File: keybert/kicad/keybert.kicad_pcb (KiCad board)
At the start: 2 copper layers, 146.8 x 123 mm, 62 parts, among them J0 TRRS

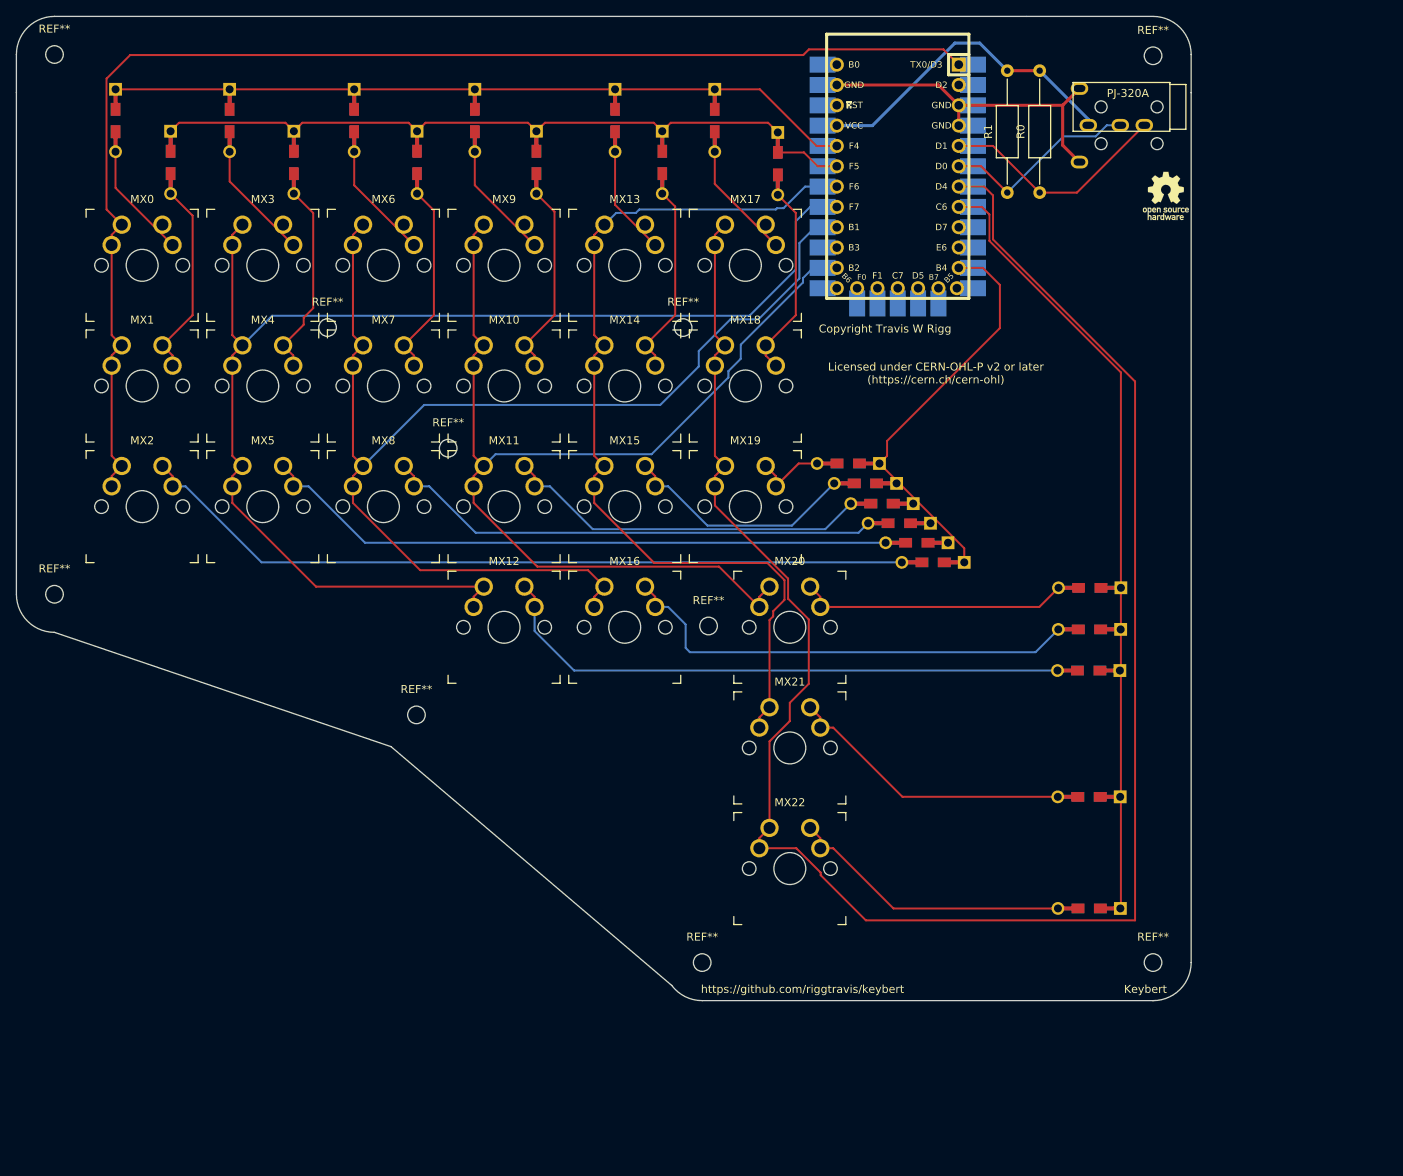
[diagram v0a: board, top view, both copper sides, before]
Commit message: feat: enforced good board geometry using FreeCAD
Parametric modeling is a wonderful thing and I'm unclear on why
KiCAD doesn't have it. Oh well, it is what is is. Using the
dimensions I obtained from the wonderful experience of performing
my parametric modeling adjustments, I finally had all of the
information I needed to get pricing for the PCBs as they are
currently designed. The results were not good. Currently,
[Aisler](https://aisler.community/t/pcb-design-rules/41) rates the
design as complex. This fails to meet the mission goal of Keybert
in a couple of ways.

Firstly, a complex PCB is an expensive PCB and an expensive PCB is
not beginner friendly. Secondly, a complex PCB is a harder to
understand and evaluate PCB and a harder to understand and evaluate
PCB is a PCB that doesn't help a biginner wrap their heads around
the sorts of decisions are present in the general world of custom
mechanical keyboards. Also, as an open source project, I feel a
certain degree of responsibility to make sure that this is as easy
to remix and remaster as possible. I look at the ecosystem left by
wootapoot and am so glad that the Let's Split was open sourced.
That board was a wonderful and excellent board, but the original
creator has seemingly vanished. I want when I stop being available
to support Keybert for Keybert to be able to venture out into the
world supported by many, just like the Let's Split lives on and
even has inspired things like the Lundquist and Let's Tango

chore: tidy up repository

Look at this place! Look at this mess! This isn't easy to understand or
explore! What are we even doing here!?

fix: moved file into correct directory

I accidentally broke all of the KiCAD files with the last commit. Now
things should be better and functional
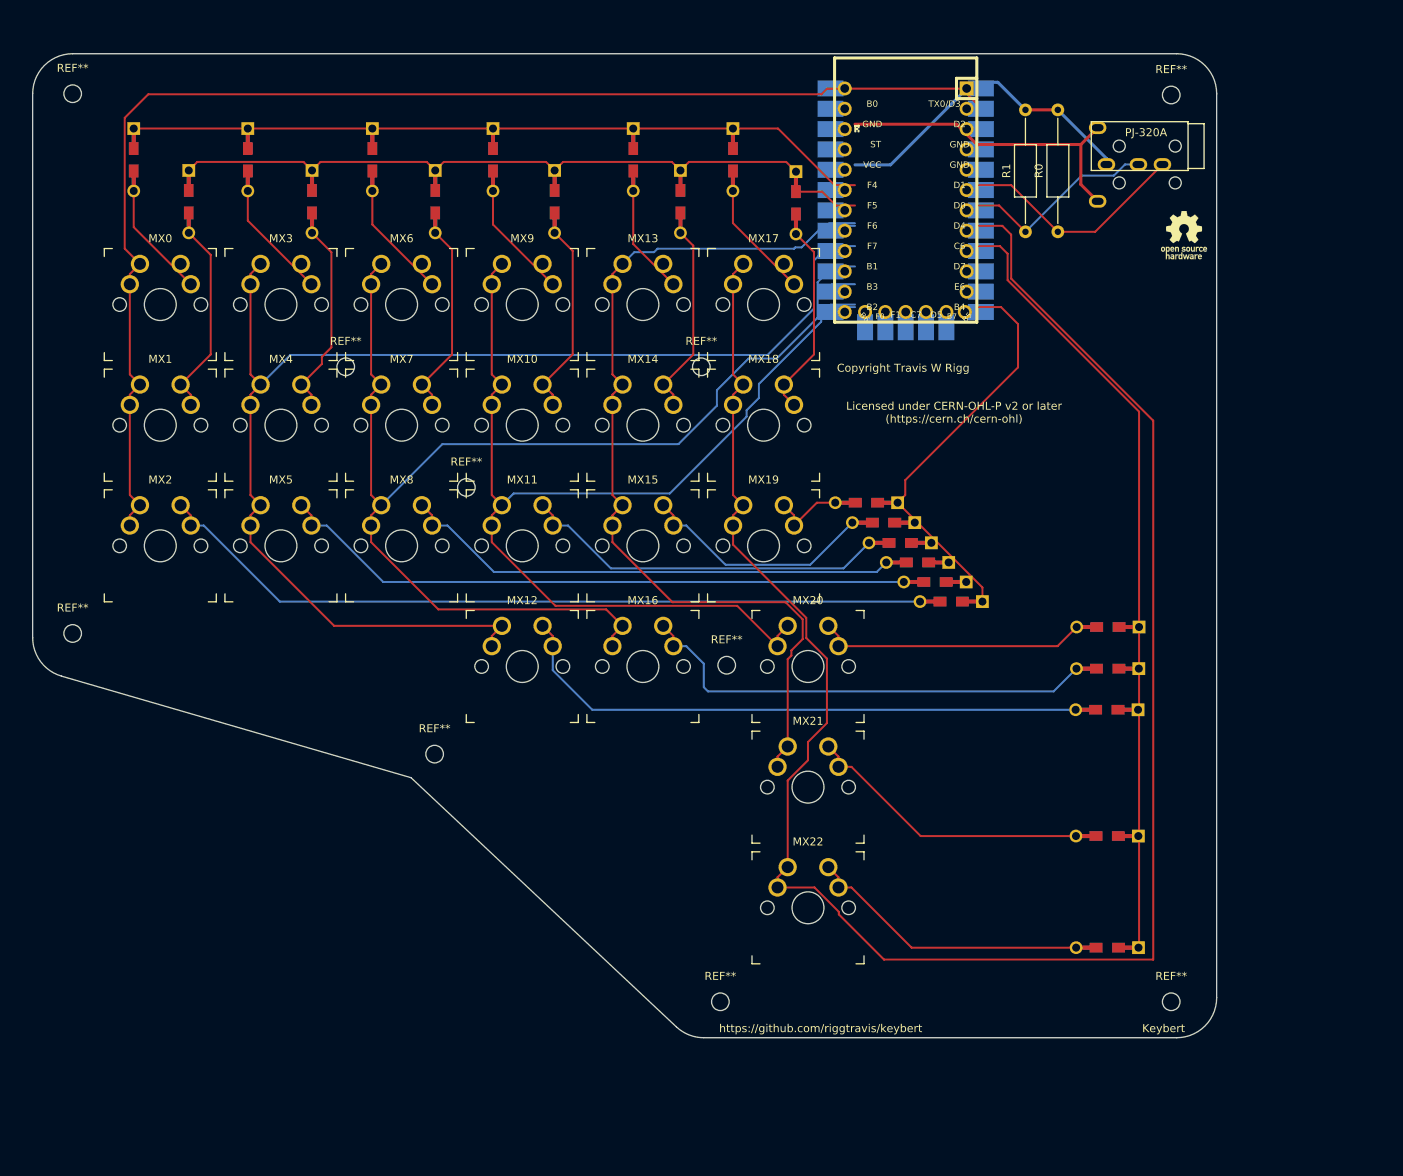
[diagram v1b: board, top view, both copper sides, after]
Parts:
- moved D12 5.40 mm to (150.8, 100.0)
- moved D15 5.40 mm to (122.8, 76.6)
- moved D17 5.40 mm to (104.0, 31.3)
- moved D2 5.40 mm to (131.3, 86.5)
- moved D22 5.40 mm to (150.8, 129.7)
- moved D5 5.40 mm to (129.3, 84.0)
- moved J0 5.40 mm to (160.9, 31.8)
- moved MX13 5.40 mm to (92.8, 49.4)
- moved MX14 5.40 mm to (92.8, 64.4)
- moved MX15 5.40 mm to (92.8, 79.5)
- moved MX16 5.40 mm to (92.8, 94.6)
- moved MX17 5.40 mm to (107.8, 49.4)
- moved MX18 5.40 mm to (107.8, 64.4)
- moved MX19 5.40 mm to (107.8, 79.5)
- moved R0 5.40 mm to (144.6, 40.3)
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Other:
- board size 146.8 x 123 mm -> 148 x 123 mm

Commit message: fix: new revision to reduce costs
Having followed the
[Aisler design rules](https://aisler.community/t/pcb-design-rules/41)
I think this new design should be cheaper
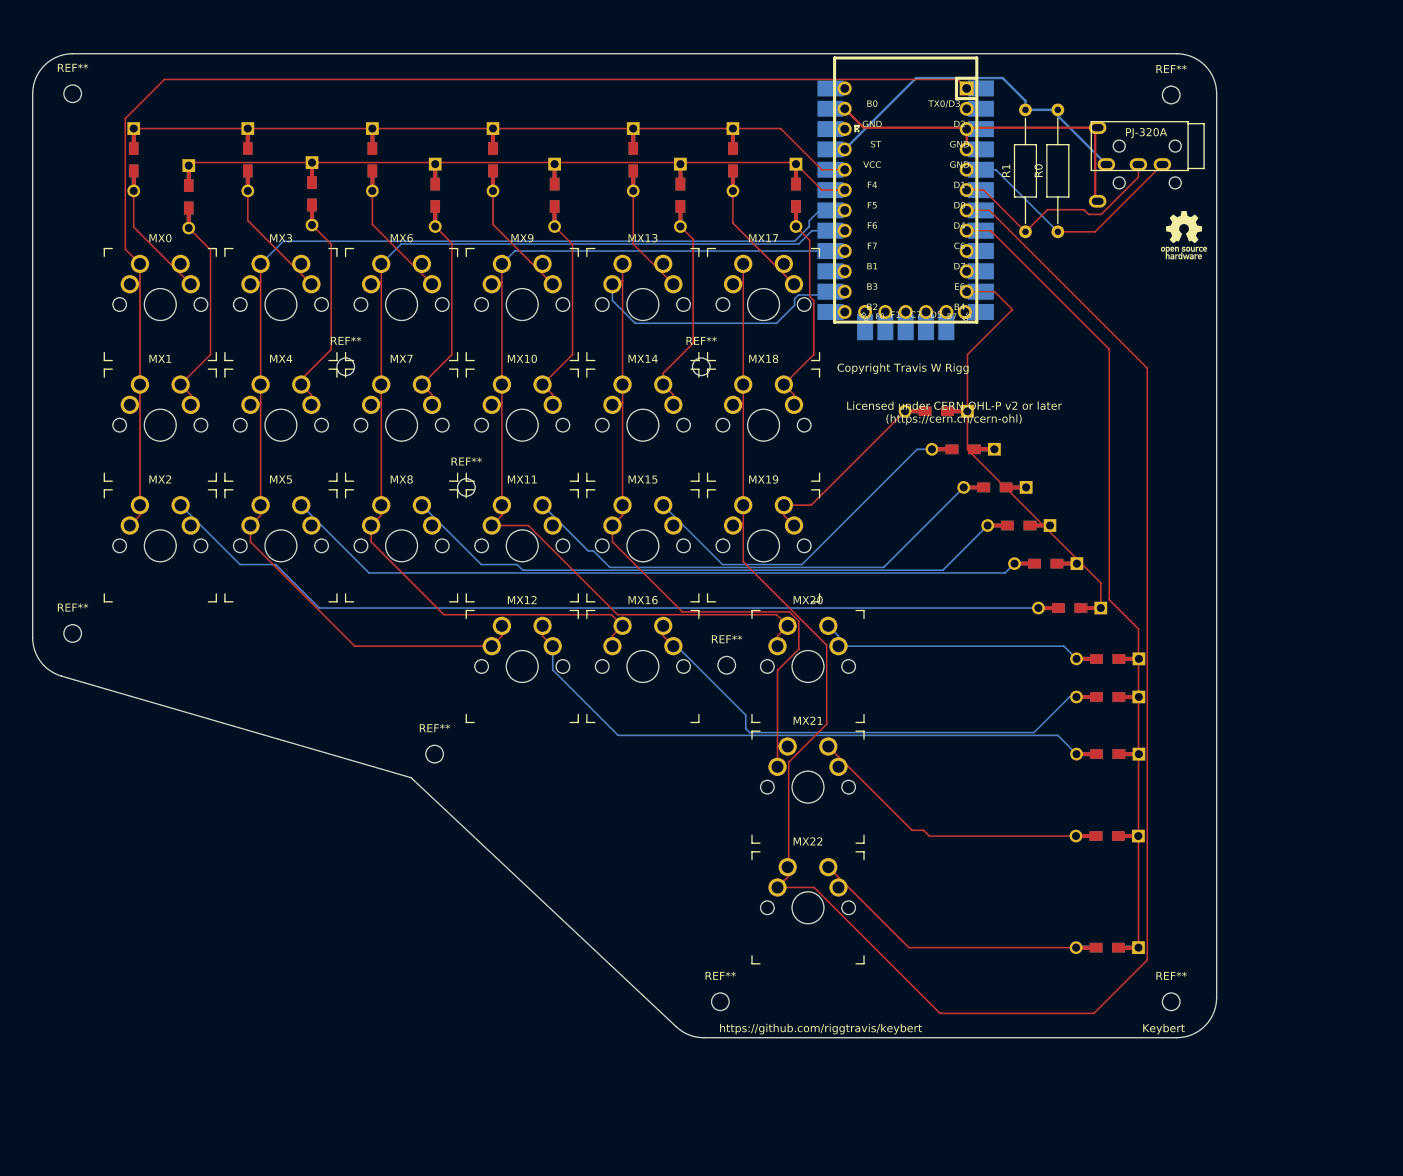
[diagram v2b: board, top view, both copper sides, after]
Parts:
- moved D2 14.8 mm to (146.1, 87.3)
- moved D19 14.4 mm to (129.4, 62.7)
- moved D5 14.0 mm to (143.1, 81.7)
- moved D11 13.7 mm to (136.8, 72.2)
- moved D15 13.5 mm to (132.8, 67.4)
- moved D8 13.5 mm to (139.7, 77.0)
- moved D12 5.55 mm to (150.9, 105.5)
- moved D20 3.98 mm to (150.9, 93.6)
- moved D16 3.54 mm to (150.9, 98.4)
- moved D4 0.98 mm to (51.4, 35.5)
- moved D18 0.94 mm to (111.9, 35.7)
- moved D10 0.79 mm to (81.7, 35.7)
- moved D14 0.79 mm to (97.5, 35.7)
- moved D7 0.79 mm to (66.8, 35.7)
- moved D1 0.60 mm to (36.0, 35.9)
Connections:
- MC-EC0 pad 14: col3 -> col4
- MC-EC0 pad 16: col2 -> col3
- MC-EC0 pad 17: col1 -> col2
- MC-EC0 pad 18: col4 -> col1
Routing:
- net col3: track 140.8 -> 124.8 mm
- net col2: track 151.5 -> 136.6 mm
- net Net-(D2-Pad2): track 98.2 -> 112.6 mm
- net Net-(D11-Pad2): track 46.1 -> 60.0 mm
- net Net-(D19-Pad2): track 9.40 -> 23.1 mm
- net Net-(D8-Pad2): track 62.7 -> 76.4 mm
- net Net-(D5-Pad2): track 80.0 -> 93.1 mm
- net Net-(D15-Pad2): track 29.7 -> 42.6 mm
- net col1: track 161.2 -> 152.9 mm
- net col5: track 241.6 -> 249.3 mm
- net row1: track 88.5 -> 83.6 mm
- net row0: track 94.7 -> 91.0 mm
- net SCL: track 25.0 -> 28.5 mm
- net unconnected-(MC-EC0-Pad15): track 2.95 -> 0.00 mm
- net clu0: track 97.7 -> 100.3 mm
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
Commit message: fix: No longer incurring complexity fee
After a lot of work, the PCB itself should now be viable for ordering.
At time of completion of that work, the PCB is $30 to be produced in the
United states in a batch of 3 or $22 to be produced in China in a batch
of 5. Arguably, that batch of five is more in line with the vision for
Keybert, however, I would forsee myself preferring the American PCB
manufacturer for my own boards given overall sociopolitical
circumstances in the world. I have decided that Keybert will exist
purely in the cheapest possible way with no guidance on how ethical or
unethical it is to engage with various entities. There likely will need
to be documentation somewhere stating outright that the creator of
Keybert in no way condones things like the Uigher genocide, the invasion
of Ukraine, or any other form of genocide

fix: added library file for TRRS jack

In order to properly work with the Keebio TRRS symbol, I needed to
create a footprint that matched it in terms of pads. Or wait no.
Otherway. I wanted to use the Keebio footprint, so I created a new
symbol to match in terms of pads
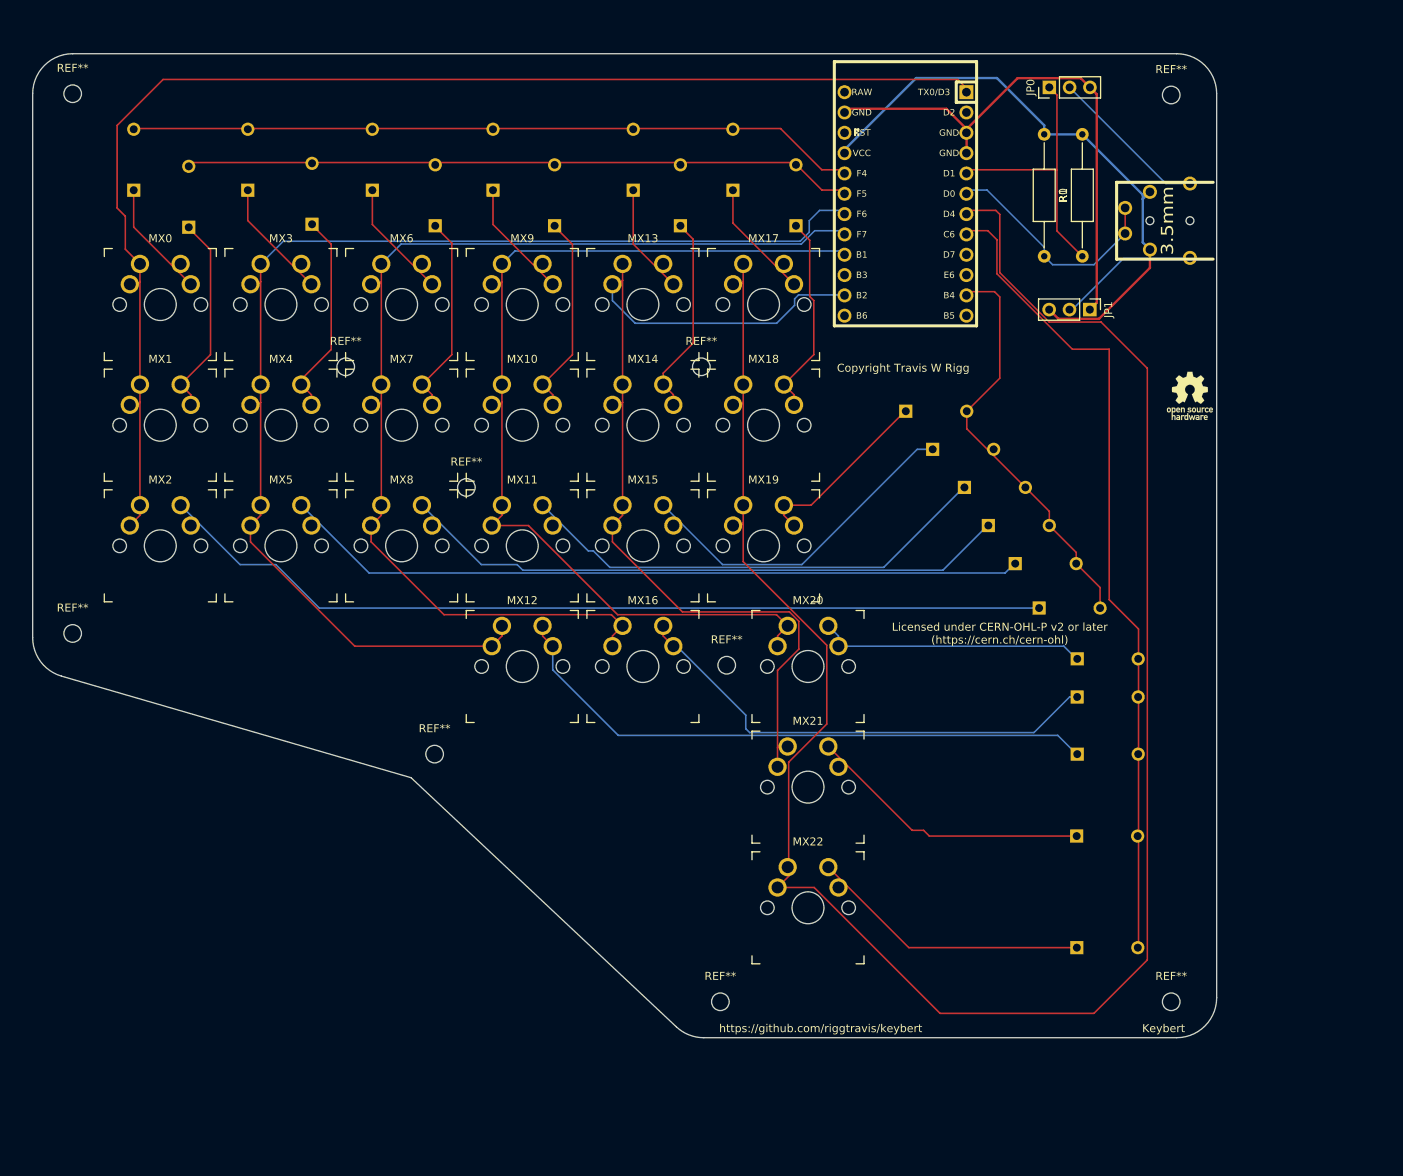
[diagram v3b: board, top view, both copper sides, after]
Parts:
- removed J0: TRRS, Keebio-Parts:TRRS-PJ-320A-dual
- removed MC-EC0: Elite-C, Keebio-Parts:Elite-C-castellated-29pin-holes
- added JP0: Jumper_3_Bridged12, Connector_PinHeader_2.54mm:PinHeader_1x03_P2.54mm_Vertical, F.Cu at (143.6, 22.2)
- added JP1: Jumper_3_Bridged12, Connector_PinHeader_2.54mm:PinHeader_1x03_P2.54mm_Vertical, F.Cu at (148.6, 50.0)
- added TRRS0: TRRS:flipped, Keebio-Parts:TRRS_Jack, F.Cu at (156.1, 38.9)
- added U0: ProMicro, Keebio-Parts:ArduinoProMicro, B.Cu at (125.6, 36.8)
- D0, D1, D10, D11, D12, D13, D14, D15, D16, D17, D18, D19, D2, D20, D21, D22, D3, D4, D5, D6, D7, D8, D9: footprint Keebio-Parts:Diode-dual -> Keebio-Parts:Diode
- moved REF** 20.1 mm to (161.2, 67.4)
- moved REF** 20.1 mm to (161.1, 60.8)
- moved R0 12.3 mm to (142.9, 28.1), turned to -90 degrees
- moved R1 7.74 mm to (147.7, 43.3)
- turned D0 to -90 degrees
- turned D1 to -90 degrees
- turned D10 to -90 degrees
- turned D11 to 180 degrees
- turned D12 to 180 degrees
- turned D13 to -90 degrees
- turned D14 to -90 degrees
- turned D15 to 180 degrees
- turned D16 to 180 degrees
- turned D17 to -90 degrees
- turned D18 to -90 degrees
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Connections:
- R0 pad 1: SDA -> VCC
- R0 pad 2: VCC -> SCL
- R1 pad 1: SCL -> SDA
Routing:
- net VCC: track 41.5 -> 74.1 mm
- net GND: track 44.6 -> 65.8 mm
- net Net-(JP0-Pad2): track 0.00 -> 20.0 mm
- net Net-(JP1-Pad2): track 0.00 -> 17.7 mm
- net col5: track 249.3 -> 253.5 mm
- net SDA: track 31.2 -> 34.1 mm
- net clu0: track 100.3 -> 102.8 mm
- net row2: track 53.2 -> 51.9 mm
- net col0: track 162.6 -> 163.6 mm
- net SCL: track 28.5 -> 29.2 mm
- net col4: track 120.5 -> 120.0 mm
